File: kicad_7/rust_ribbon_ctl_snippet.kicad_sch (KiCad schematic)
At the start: 8 parts, among them U1 STM32L031F4Px, U2 MCP4822

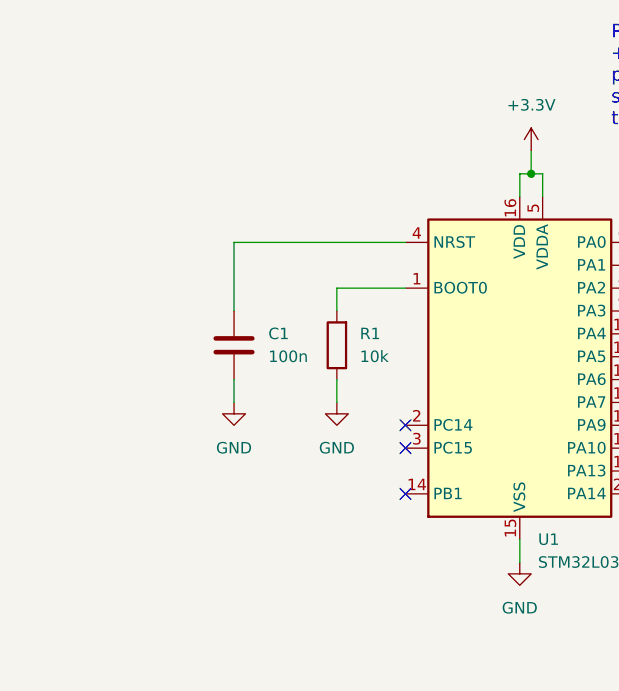
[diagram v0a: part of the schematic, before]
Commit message: Add mode switch with 3 MIDI note modes
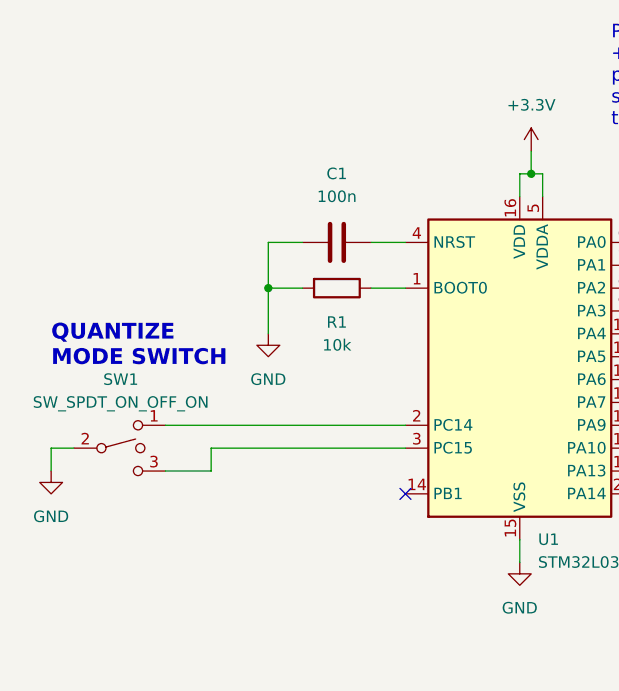
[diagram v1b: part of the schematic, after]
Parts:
- added SW1: SW_SPDT_ON_OFF_ON, symbol Switch:SW_SPDT_MSM
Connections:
- net GND: now also C1.2, R1.2, SW1.2; no longer C1.1, R1.1
- net at U1.1 (BOOT0): now also R1.1; no longer R1.2
- net at U1.2 (PC14): now also SW1.1
- net at U1.3 (PC15): now also SW1.3
- net at U1.4 (NRST): now also C1.1; no longer C1.2
- no-connect marks 9 -> 7
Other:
- note added: "QUANTIZE MODE SWITCH"
- moved on the sheet: C1, R1
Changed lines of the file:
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@@
     (comment 3 "Author: Jordan Aceto")
+  )
+  (junction (at 80.01 87.63) (diameter 0) (color 0 0 0 0)
   )
   (junction (at 163.83 82.55) (diameter 0) (color 0 0 0 0)
@@
   (no_connect (at 120.65 90.17))
   (no_connect (at 95.25 110.49))
-  (no_connect (at 95.25 102.87))
   (no_connect (at 120.65 107.95))
   (no_connect (at 120.65 105.41))
-  (no_connect (at 95.25 105.41))
   (wire (pts (xy 120.65 92.71) (xy 130.81 92.71))
     (stroke (width 0) (type default))
   )
-  (wire (pts (xy 87.63 97.79) (xy 87.63 100.33))
-    (stroke (width 0) (type default))
-  )
   (wire (pts (xy 180.34 82.55) (xy 163.83 82.55))
     (stroke (width 0) (type default))
   )
-  (wire (pts (xy 76.2 90.17) (xy 76.2 82.55))
+  (wire (pts (xy 80.01 82.55) (xy 80.01 87.63))
     (stroke (width 0) (type default))
   )
@@
     (stroke (width 0) (type default))
   )
+  (wire (pts (xy 68.58 102.87) (xy 95.25 102.87))
+    (stroke (width 0) (type default))
+  )
   (wire (pts (xy 200.66 123.19) (xy 205.74 123.19))
     (stroke (width 0) (type default))
@@
     (stroke (width 0) (type default))
   )
-  (wire (pts (xy 87.63 90.17) (xy 87.63 87.63))
+  (wire (pts (xy 80.01 87.63) (xy 80.01 92.71))
     (stroke (width 0) (type default))
   )
@@
     (stroke (width 0) (type default))
   )
+  (wire (pts (xy 68.58 107.95) (xy 73.66 107.95))
+    (stroke (width 0) (type default))
+  )
   (wire (pts (xy 151.13 102.87) (xy 151.13 87.63))
     (stroke (width 0) (type default))
@@
     (stroke (width 0) (type default))
   )
+  (wire (pts (xy 73.66 105.41) (xy 95.25 105.41))
+    (stroke (width 0) (type default))
+  )
+  (wire (pts (xy 91.44 82.55) (xy 95.25 82.55))
+    (stroke (width 0) (type default))
+  )
   (wire (pts (xy 177.8 78.74) (xy 180.34 78.74))
     (stroke (width 0) (type default))
@@
     (stroke (width 0) (type default))
   )
-  (wire (pts (xy 87.63 87.63) (xy 95.25 87.63))
+  (wire (pts (xy 91.44 87.63) (xy 95.25 87.63))
     (stroke (width 0) (type default))
   )
@@
     (stroke (width 0) (type default))
   )
+  (wire (pts (xy 55.88 105.41) (xy 55.88 107.95))
+    (stroke (width 0) (type default))
+  )
   (wire (pts (xy 120.65 82.55) (xy 151.13 82.55))
     (stroke (width 0) (type default))
@@
     (stroke (width 0) (type default))
   )
-  (wire (pts (xy 76.2 97.79) (xy 76.2 100.33))
-    (stroke (width 0) (type default))
-  )
   (wire (pts (xy 187.96 140.97) (xy 187.96 138.43))
     (stroke (width 0) (type default))
   )
+  (wire (pts (xy 80.01 87.63) (xy 83.82 87.63))
+    (stroke (width 0) (type default))
+  )
+  (wire (pts (xy 55.88 105.41) (xy 58.42 105.41))
+    (stroke (width 0) (type default))
+  )
+  (wire (pts (xy 73.66 107.95) (xy 73.66 105.41))
+    (stroke (width 0) (type default))
+  )
   (wire (pts (xy 110.49 77.47) (xy 110.49 74.93))
     (stroke (width 0) (type default))
@@
     (stroke (width 0) (type default))
   )
-  (wire (pts (xy 76.2 82.55) (xy 95.25 82.55))
+  (wire (pts (xy 80.01 82.55) (xy 83.82 82.55))
     (stroke (width 0) (type default))
   )
@@
   (wire (pts (xy 107.95 115.57) (xy 107.95 118.11))
     (stroke (width 0) (type default))
+  )
+  (text "QUANTIZE\nMODE SWITCH" (at 55.88 96.52 0)
+    (effects (font (size 1.75 1.75) (thickness 0.35) bold) (justify left bottom))
   )
   (text "Pull the ribbon up towards \n+5v but clamp at +3v3. This \nprovides a little noise immumity\nso we can detect levels close\nto the top of the range."
@@
     (effects (font (size 1.27 1.27)) (justify left))
   )
-  (symbol (lib_id "power:GND") (at 76.2 100.33 0) (unit 1)
-    (in_bom yes) (on_board yes) (dnp no) (fields_autoplaced)
-    (property "Reference" "#PWR?" (at 76.2 106.68 0)
-      (effects (font (size 1.27 1.27)) hide)
-    )
-    (property "Value" "GND" (at 76.2 105.41 0)
-      (effects (font (size 1.27 1.27)))
-    )
-    (property "Footprint" "" (at 76.2 100.33 0)
-      (effects (font (size 1.27 1.27)) hide)
-    )
-    (property "Datasheet" "" (at 76.2 100.33 0)
+  (symbol (lib_id "power:GND") (at 80.01 92.71 0) (unit 1)
+    (in_bom yes) (on_board yes) (dnp no) (fields_autoplaced)
+    (property "Reference" "#PWR?" (at 80.01 99.06 0)
+      (effects (font (size 1.27 1.27)) hide)
+    )
+    (property "Value" "GND" (at 80.01 97.79 0)
+      (effects (font (size 1.27 1.27)))
+    )
+    (property "Footprint" "" (at 80.01 92.71 0)
+      (effects (font (size 1.27 1.27)) hide)
+    )
+    (property "Datasheet" "" (at 80.01 92.71 0)
       (effects (font (size 1.27 1.27)) hide)
     )
@@
     )
   )
-  (symbol (lib_id "Device:R") (at 87.63 93.98 180) (unit 1)
-    (in_bom yes) (on_board yes) (dnp no) (fields_autoplaced)
-    (property "Reference" "R1" (at 90.17 92.7099 0)
-      (effects (font (size 1.27 1.27)) (justify right))
-    )
-    (property "Value" "10k" (at 90.17 95.2499 0)
-      (effects (font (size 1.27 1.27)) (justify right))
-    )
-    (property "Footprint" "Resistor_SMD:R_0805_2012Metric" (at 89.408 93.98 90)
-      (effects (font (size 1.27 1.27)) hide)
-    )
-    (property "Datasheet" "~" (at 87.63 93.98 0)
+  (symbol (lib_id "Device:R") (at 87.63 87.63 270) (unit 1)
+    (in_bom yes) (on_board yes) (dnp no) (fields_autoplaced)
+    (property "Reference" "R1" (at 87.63 91.44 90)
+      (effects (font (size 1.27 1.27)))
+    )
+    (property "Value" "10k" (at 87.63 93.98 90)
+      (effects (font (size 1.27 1.27)))
+    )
+    (property "Footprint" "Resistor_SMD:R_0805_2012Metric" (at 87.63 85.852 90)
+      (effects (font (size 1.27 1.27)) hide)
+    )
+    (property "Datasheet" "~" (at 87.63 87.63 0)
       (effects (font (size 1.27 1.27)) hide)
     )
@@
     )
   )
+  (symbol (lib_id "power:GND") (at 55.88 107.95 0) (unit 1)
+    (in_bom yes) (on_board yes) (dnp no) (fields_autoplaced)
+    (property "Reference" "#PWR0101" (at 55.88 114.3 0)
+      (effects (font (size 1.27 1.27)) hide)
+    )
+    (property "Value" "GND" (at 55.88 113.03 0)
+      (effects (font (size 1.27 1.27)))
+    )
+    (property "Footprint" "" (at 55.88 107.95 0)
+      (effects (font (size 1.27 1.27)) hide)
+    )
+    (property "Datasheet" "" (at 55.88 107.95 0)
+      (effects (font (size 1.27 1.27)) hide)
+    )
+    (pin "1")
+    (instances
+      (project "rust_ribbon_ctl_snippet"
+        (path "/a073cccf-103c-4731-a193-343bc5f8220d"
+          (reference "#PWR0101") (unit 1)
+        )
+      )
+    )
+  )
   (symbol (lib_id "Device:D_Schottky") (at 151.13 72.39 90) (mirror x) (unit 1)
     (in_bom yes) (on_board yes) (dnp no) (fields_autoplaced)
@@
     )
   )
-  (symbol (lib_id "Device:C") (at 76.2 93.98 180) (unit 1)
-    (in_bom yes) (on_board yes) (dnp no) (fields_autoplaced)
-    (property "Reference" "C1" (at 80.01 92.7099 0)
-      (effects (font (size 1.27 1.27)) (justify right))
-    )
-    (property "Value" "100n" (at 80.01 95.2499 0)
-      (effects (font (size 1.27 1.27)) (justify right))
-    )
-    (property "Footprint" "Capacitor_SMD:C_0805_2012Metric" (at 75.2348 90.17 0)
-      (effects (font (size 1.27 1.27)) hide)
-    )
-    (property "Datasheet" "~" (at 76.2 93.98 0)
+  (symbol (lib_id "Device:C") (at 87.63 82.55 270) (unit 1)
+    (in_bom yes) (on_board yes) (dnp no) (fields_autoplaced)
+    (property "Reference" "C1" (at 87.63 74.93 90)
+      (effects (font (size 1.27 1.27)))
+    )
+    (property "Value" "100n" (at 87.63 77.47 90)
+      (effects (font (size 1.27 1.27)))
+    )
+    (property "Footprint" "Capacitor_SMD:C_0805_2012Metric" (at 83.82 83.5152 0)
+      (effects (font (size 1.27 1.27)) hide)
+    )
+    (property "Datasheet" "~" (at 87.63 82.55 0)
       (effects (font (size 1.27 1.27)) hide)
     )
@@
     )
   )
+  (symbol (lib_id "Switch:SW_SPDT_MSM") (at 63.5 105.41 0) (unit 1)
+    (in_bom yes) (on_board yes) (dnp no) (fields_autoplaced)
+    (property "Reference" "SW1" (at 63.627 97.79 0)
+      (effects (font (size 1.27 1.27)))
+    )
+    (property "Value" "SW_SPDT_ON_OFF_ON" (at 63.627 100.33 0)
+      (effects (font (size 1.27 1.27)))
+    )
+    (property "Footprint" "" (at 63.5 105.41 0)
+      (effects (font (size 1.27 1.27)) hide)
+    )
+    (property "Datasheet" "~" (at 63.5 105.41 0)
+      (effects (font (size 1.27 1.27)) hide)
+    )
+    (pin "1")
+    (pin "2")
+    (pin "3")
+    (instances
+      (project "rust_ribbon_ctl_snippet"
+        (path "/a073cccf-103c-4731-a193-343bc5f8220d"
+          (reference "SW1") (unit 1)
+        )
+      )
+    )
+  )
   (symbol (lib_id "power:+3.3V") (at 151.13 66.04 0) (mirror y) (unit 1)
     (in_bom yes) (on_board yes) (dnp no) (fields_autoplaced)
@@
       (effects (font (size 1.27 1.27)) hide)
     )
-    (pin "1")
-    (instances
-      (project "rust_ribbon_ctl_snippet"
-        (path "/a073cccf-103c-4731-a193-343bc5f8220d"
-          (reference "#PWR?") (unit 1)
-        )
-      )
-    )
-  )
-  (symbol (lib_id "power:GND") (at 87.63 100.33 0) (unit 1)
-    (in_bom yes) (on_board yes) (dnp no) (fields_autoplaced)
-    (property "Reference" "#PWR?" (at 87.63 106.68 0)
-      (effects (font (size 1.27 1.27)) hide)
-    )
-    (property "Value" "GND" (at 87.63 105.41 0)
-      (effects (font (size 1.27 1.27)))
-    )
-    (property "Footprint" "" (at 87.63 100.33 0)
-      (effects (font (size 1.27 1.27)) hide)
-    )
-    (property "Datasheet" "" (at 87.63 100.33 0)
-      (effects (font (size 1.27 1.27)) hide)
-    )
